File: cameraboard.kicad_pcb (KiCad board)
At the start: 4 copper layers, 47.2 x 46.8 mm, 93 parts, among them J1 USB_C_Receptacle_USB2.0, J2 02x05 M 1.27mm, J4 F32R-1A7H1-11024, J6 TFM-110-12-L-D-A, J7 FLE-107-01-G-DV-A, J8 USD-1040310811, Q1 SQ3495EV-T1, Q2 DMP6350SQ-7, SW1 CAS-120TA, SW2 KMR2x, SW4 CAS-120TA, U1 STM32H743VITx, U2 WE-TVS-82400102, U3 XC6210B332MR-G, U4 AP7366-28W5-7, U5 ?, U6 LTC4412xS6, Y1 16MHz

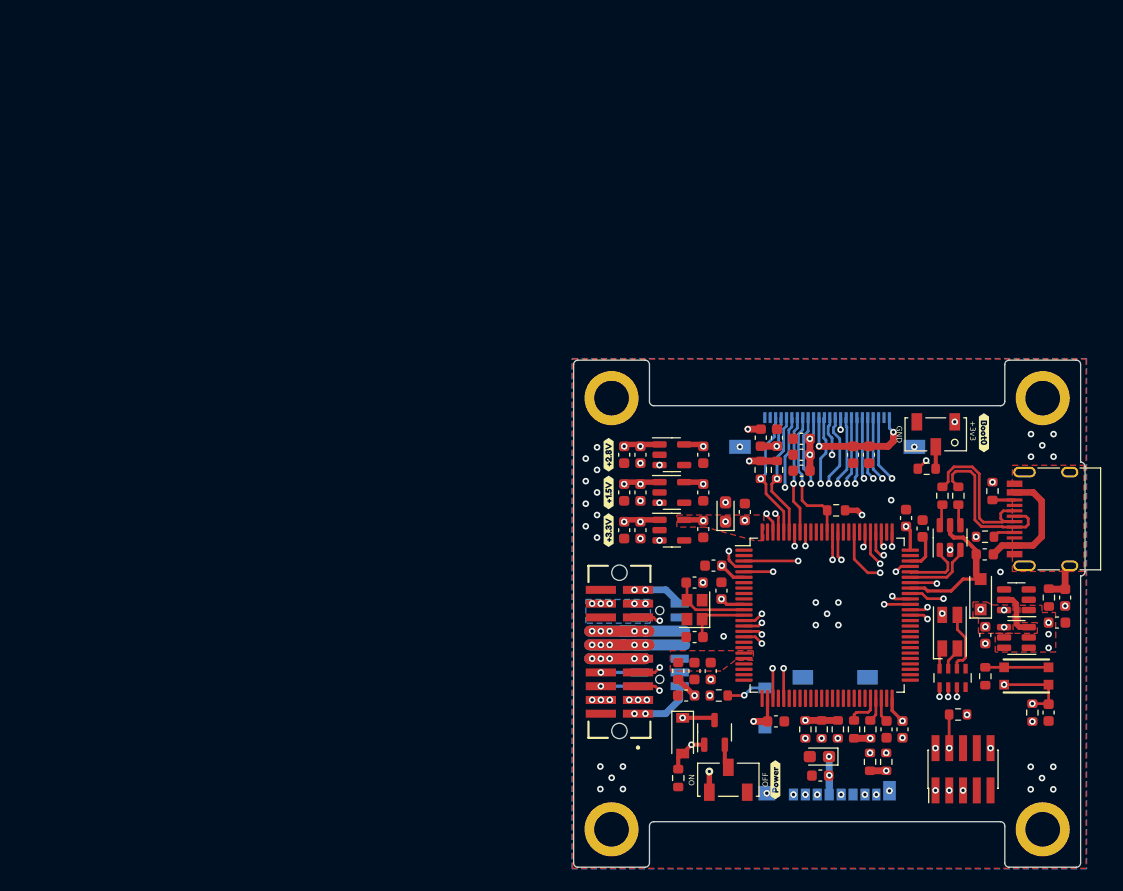
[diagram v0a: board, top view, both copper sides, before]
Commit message: Simplified Enable Circuit
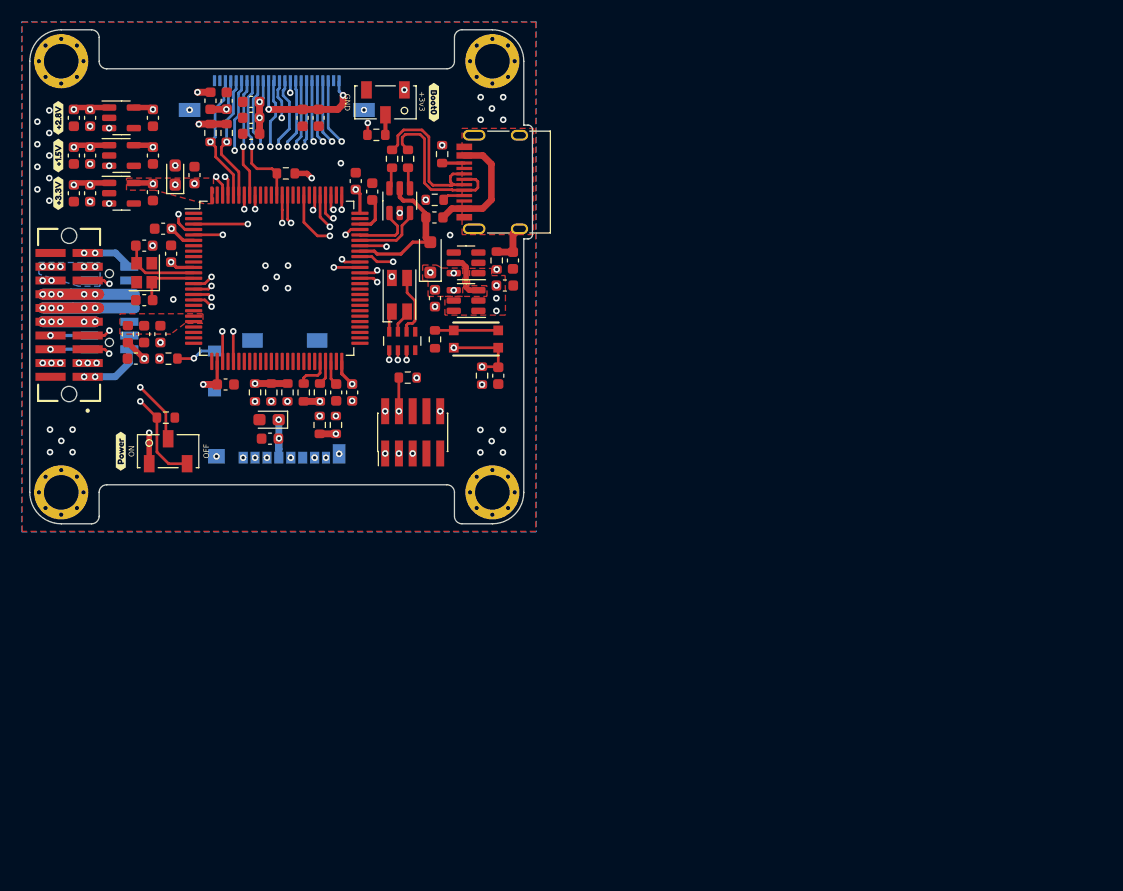
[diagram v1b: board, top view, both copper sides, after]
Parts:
- removed the D2 at (140.5, 108.6)
- removed Q2: DMP6350SQ-7, Package_TO_SOT_SMD:SOT-23-3
- J4: value F32R-1A7H1-11024 -> MOLEX_5051102491; footprint cameraboard:5051102491 -> cameraboard:MOLEX_5051102491
- J6: value TFM-110-12-L-D-A -> TFM-110-12-X-D-A; footprint cameraboard:SAMTEC_TFM-110-12-L-D-A -> mainboard:SAMTEC_TFM-110-12-X-D-A
- J7: value FLE-107-01-G-DV-A -> FLE-107-01-X-DV-A; footprint cameraboard:SAMTEC_FLE-107-01-G-DV-A -> cameraboard:SAMTEC_FLE-107-01-X-DV-A
- R9: value 100K -> 10K
- SW2: footprint mainboard:BTN_KMR2_4.6X2.8 -> mainboard:BTN_KMR2
- U5: value ? -> TLV75515PDBVR
- moved kibuzzard-63E3EAF3 67.6 mm to (88.6, 82.3)
- moved SW3 59.9 mm to (93.0, 82.3)
- moved C14 59.7 mm to (124.0, 67.0)
- moved C35 59.7 mm to (124.8, 64.7)
- moved R4 59.7 mm to (123.3, 64.7)
- moved C1 59.6 mm to (93.6, 56.8)
- moved C10 59.6 mm to (92.3, 71.5)
- moved C11 59.6 mm to (90.8, 71.5)
- moved C12 59.6 mm to (90.0, 73.8)
- moved C13 59.6 mm to (123.4, 75.3)
- moved C17 59.6 mm to (90.8, 68.4)
- moved C18 59.6 mm to (84.3, 58.5)
- moved C2 59.6 mm to (110.3, 57.4)
- moved C21 59.6 mm to (85.8, 58.5)
- moved C23 59.6 mm to (106.9, 51.5)
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- renumbered D3 to D2, SW4 to SW3
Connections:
- J4 pad P1: GND -> (no net)
- J4 pad P2: GND -> (no net)
- SW3 pad 2: Net-(SW4-Pad2) -> /POWER_EN
- SW3 pad 3: GND -> /PAYLOAD_EN
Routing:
- net /POWER_EN: track 27.2 -> 30.9 mm
- net /PAYLOAD_EN: track 18.8 -> 22.4 mm
- net Net-(SW4-Pad2): track 2.22 -> 0.00 mm
- net /HI_POW: track 11.2 -> 12.6 mm
- net /BOOT0: track 21.1 -> 19.9 mm
- net /BATT_P_SW: track 15.7 -> 14.9 mm
- net /DC+: track 15.6 -> 15.0 mm
- net /BATT_N_SW: track 17.0 -> 16.4 mm
- net /3V3_MB: track 11.5 -> 10.9 mm
- net GND: vias 57 -> 59
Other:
- board size 47.2 x 46.8 mm -> 46.4 x 45.6 mm
- board text added: "18-FEB-23"
- board text removed: "08-FEB-23"

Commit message: Stash before changes
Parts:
- R1: value 100 -> 100R
- R5, R8: value 22 -> 22R
- moved C19 8.84 mm to (111.1, 80.1), turned to -90 degrees
- moved R12 7.42 mm to (106.3, 82.1), turned to 0 degrees
- moved C20 7.22 mm to (109.5, 79.8), turned to 90 degrees
- moved R19 6.54 mm to (98.3, 77.6)
- moved R11 5.69 mm to (102.8, 79.1), turned to 0 degrees
- moved R13 5.30 mm to (106.3, 80.6), turned to 0 degrees
- moved R21 4.71 mm to (102.8, 77.6), turned to 0 degrees
- moved R20 3.18 mm to (106.3, 79.1), turned to 0 degrees
- moved J8 1.06 mm to (103.0, 78.5), turned to 90 degrees
- moved C4 0.36 mm to (108.1, 76.9)
- moved C3 0.36 mm to (109.6, 76.9)
- moved R17 0.33 mm to (106.7, 76.9)
- moved R15 0.31 mm to (105.2, 76.9)
- moved R10 0.18 mm to (115.3, 75.5)
- moved J2 0.15 mm to (115.7, 80.5)
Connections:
- J4 pad P1: (no net) -> GND
- J4 pad P2: (no net) -> GND
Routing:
- net /SDIO_D1: track 20.7 -> 31.1 mm, vias 3 -> 2
- net /SDIO_D0: track 20.7 -> 25.6 mm, vias 3 -> 2
- net /SDIO_D2: track 28.4 -> 32.9 mm, vias 3 -> 2
- net /SDIO_D3: track 28.0 -> 31.1 mm, vias 3 -> 2
- net /SDIO_CMD: track 28.3 -> 30.8 mm, vias 3 -> 2
- net +3.3V: track 31.6 -> 34.0 mm, vias 22 -> 24
- net /SD_CD: track 27.5 -> 28.9 mm, vias 2 -> 3
- net /SDIO_CLK: track 26.6 -> 25.4 mm
- net /SWCLK: track 24.4 -> 25.3 mm
- net GND: vias 59 -> 56

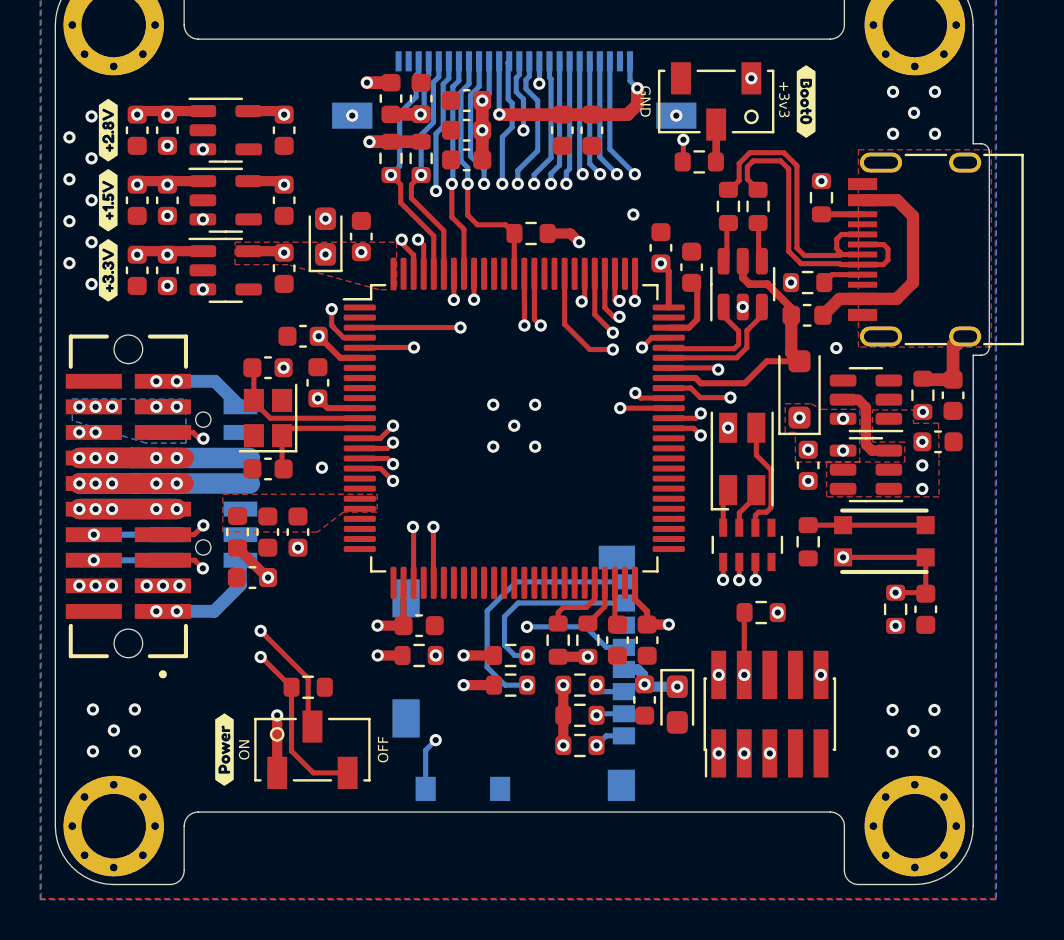
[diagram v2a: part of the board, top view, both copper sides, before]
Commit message: Moved SWD header and power switch to prevent mechanical interference
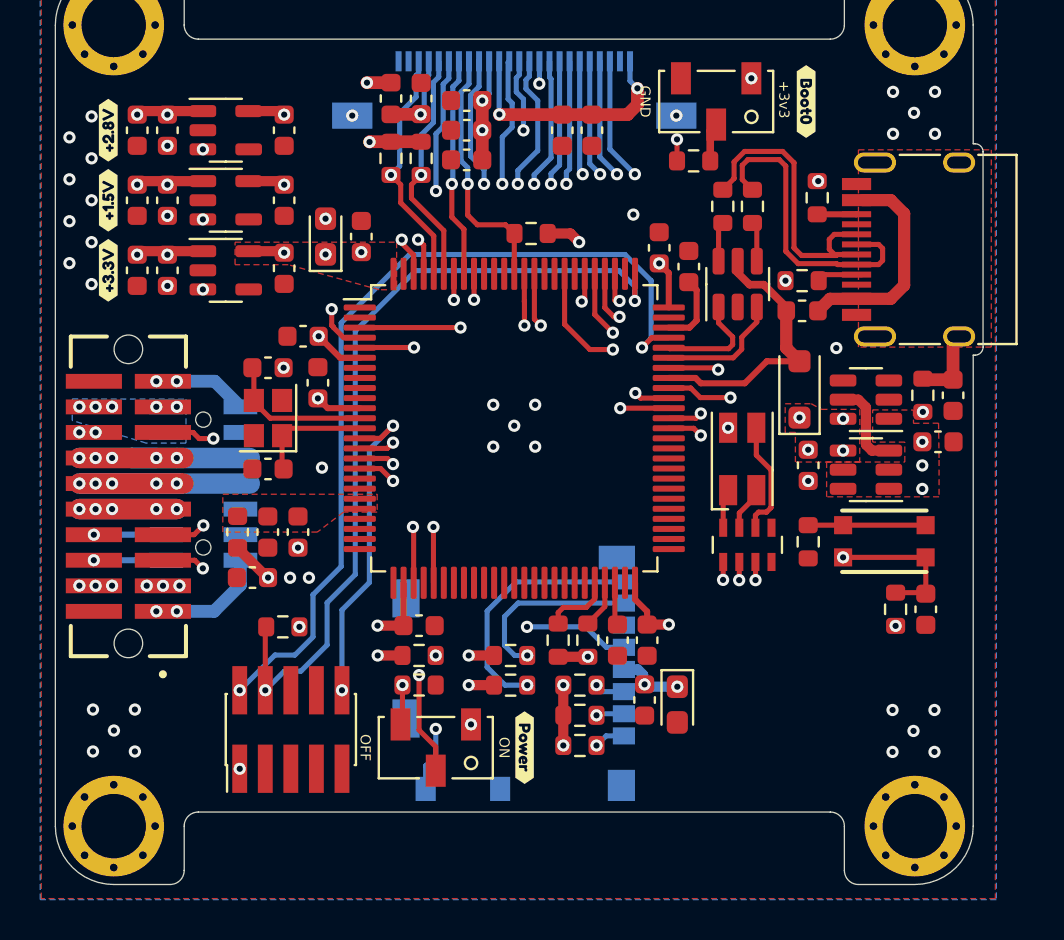
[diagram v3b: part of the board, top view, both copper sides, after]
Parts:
- moved J2 23.8 mm to (91.9, 81.3)
- moved R10 23.8 mm to (91.5, 76.2)
- moved kibuzzard-63E3EAF3 14.9 mm to (103.5, 82.2), turned to -90 degrees
- moved SW3 6.13 mm to (99.1, 82.2), turned to 180 degrees
- moved R9 5.51 mm to (98.3, 79.1)
- moved FB2 0.33 mm to (117.3, 60.5)
- moved J1 0.30 mm to (124.0, 57.5)
- moved R6 0.29 mm to (117.3, 59.0)
- moved R2 0.29 mm to (111.9, 53.0)
- moved R5 0.28 mm to (113.4, 55.3)
- moved R8 0.28 mm to (114.8, 55.3)
- moved U2 0.25 mm to (114.1, 59.2)
- moved R7 0.21 mm to (118.0, 54.9)
- moved C6 0.14 mm to (111.7, 58.3)
- moved C2 0.09 mm to (110.2, 57.4)
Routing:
- net /SWDIO: track 19.4 -> 43.3 mm
- net /SWCLK: track 25.3 -> 40.9 mm
- net /NRST: track 40.8 -> 48.5 mm, vias 4 -> 3
- net /POWER_EN: track 30.9 -> 36.0 mm, vias 4 -> 5
- net /HI_POW: track 12.6 -> 9.26 mm
- net /DC+: track 15.0 -> 16.4 mm
- net /PAYLOAD_EN: track 22.4 -> 21.3 mm, vias 2 -> 3
- net Net-(J1-SHIELD): track 3.79 -> 3.18 mm
- net Net-(FB2-Pad1): track 11.3 -> 10.7 mm
- net GND: vias 56 -> 53
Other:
- board size 46.4 x 45.6 mm -> 46.1 x 45.6 mm

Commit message: Exported Gerbers
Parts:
- renumbered J8 to J3, J6 to J5, J7 to J6
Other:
- board text added: "Bootloader"
- board text added: "MB Enable"
- board text added: "Normal"
- board text added: "On"
- board text removed: "+3v3"
- board text removed: "GND"
- board text removed: "OFF"
- board text removed: "ON"

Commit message: Rev B3/02 updates
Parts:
- removed the FB2 at (117.3, 60.5)
- removed the R5 at (113.4, 55.3)
- removed the R8 at (114.8, 55.3)
- added R20: 0R, Resistor_SMD:R_0603_1608Metric, F.Cu at (117.3, 60.5)
- added REF**: Fiducial_1mm_Mask2mm, Fiducial:Fiducial_1mm_Mask2mm, F.Cu at (122.9, 82.1)
- added REF**: Fiducial_1mm_Mask2mm, Fiducial:Fiducial_1mm_Mask2mm, F.Cu at (122.9, 50.3)
- added REF**: Fiducial_1mm_Mask2mm, Fiducial:Fiducial_1mm_Mask2mm, F.Cu at (83.1, 82.1)
- added REF**: Fiducial_1mm_Mask2mm, Fiducial:Fiducial_1mm_Mask2mm, B.Cu at (122.9, 50.3)
- added REF**: Fiducial_1mm_Mask2mm, Fiducial:Fiducial_1mm_Mask2mm, B.Cu at (122.9, 82.1)
- added REF**: Fiducial_1mm_Mask2mm, Fiducial:Fiducial_1mm_Mask2mm, B.Cu at (83.1, 82.1)
- C16, C17: value 10pF -> 4pF
- Ref**: moved to F.Cu
- Y1: value 16MHz -> 12MHz/7pF
- moved Ref** 18.3 mm to (116.2, 76.3)
- renumbered FB3 to FB2, R4 to R1, R20 to R10, R21 to R11, R11 to R12, R12 to R13, R13 to R14, R14 to R15, R15 to R17, R17 to R18, R18 to R19, R6 to R2, R7 to R3, R1 to R4, R3 to R5, R2 to R6, R9 to R7, R10 to R8, R19 to R9
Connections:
- J1 pad A6: /DC+ -> /D+
- J1 pad A7: /DC- -> /D-
- J1 pad B6: /DC+ -> /D+
- J1 pad B7: /DC- -> /D-
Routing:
- net /DC+: track 16.4 -> 0.00 mm
- net /DC-: track 15.2 -> 0.00 mm
- net /D+: track 1.99 -> 15.7 mm
- net /D-: track 1.69 -> 14.5 mm
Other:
- board text added: "12-APR-23"
- board text added: "Rev B3/02"
- board text removed: "18-FEB-23"
- board text removed: "Rev B3/01"

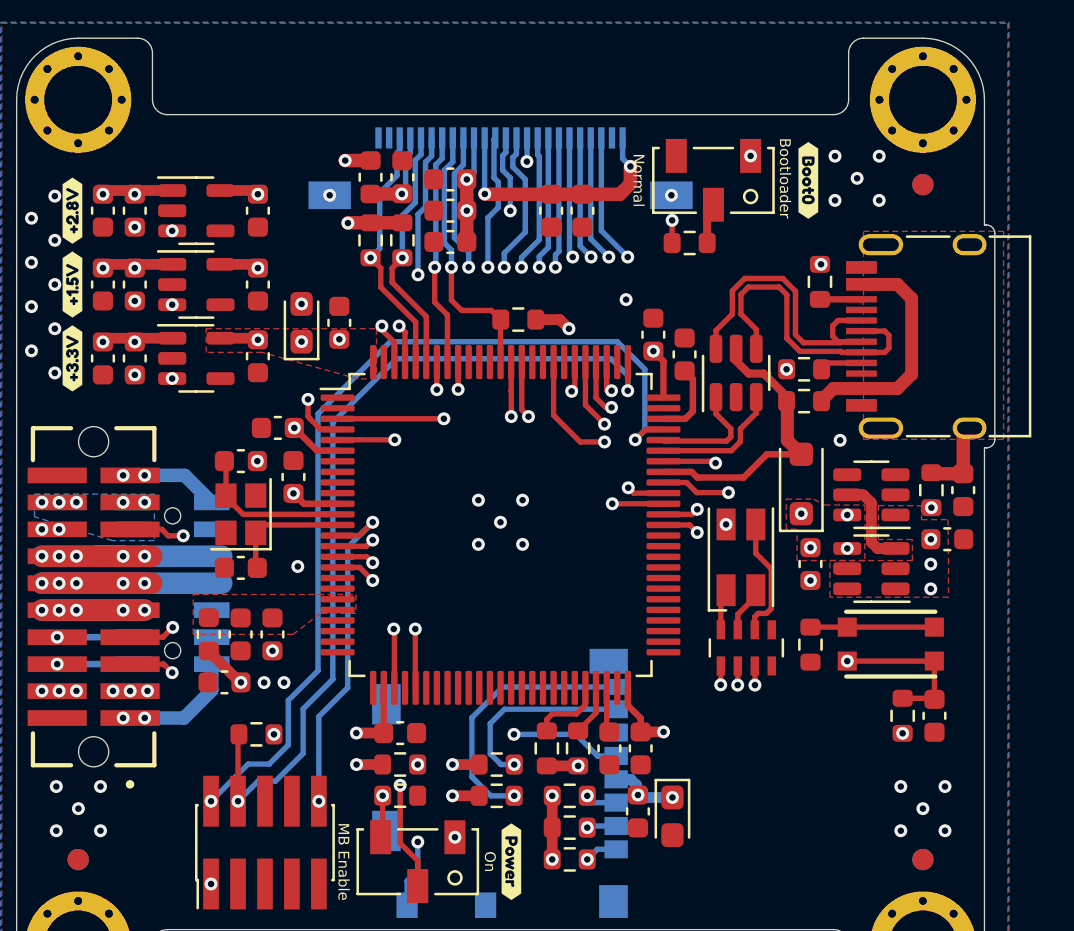
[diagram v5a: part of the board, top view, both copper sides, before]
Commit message: Rewired UART lines to mainboard
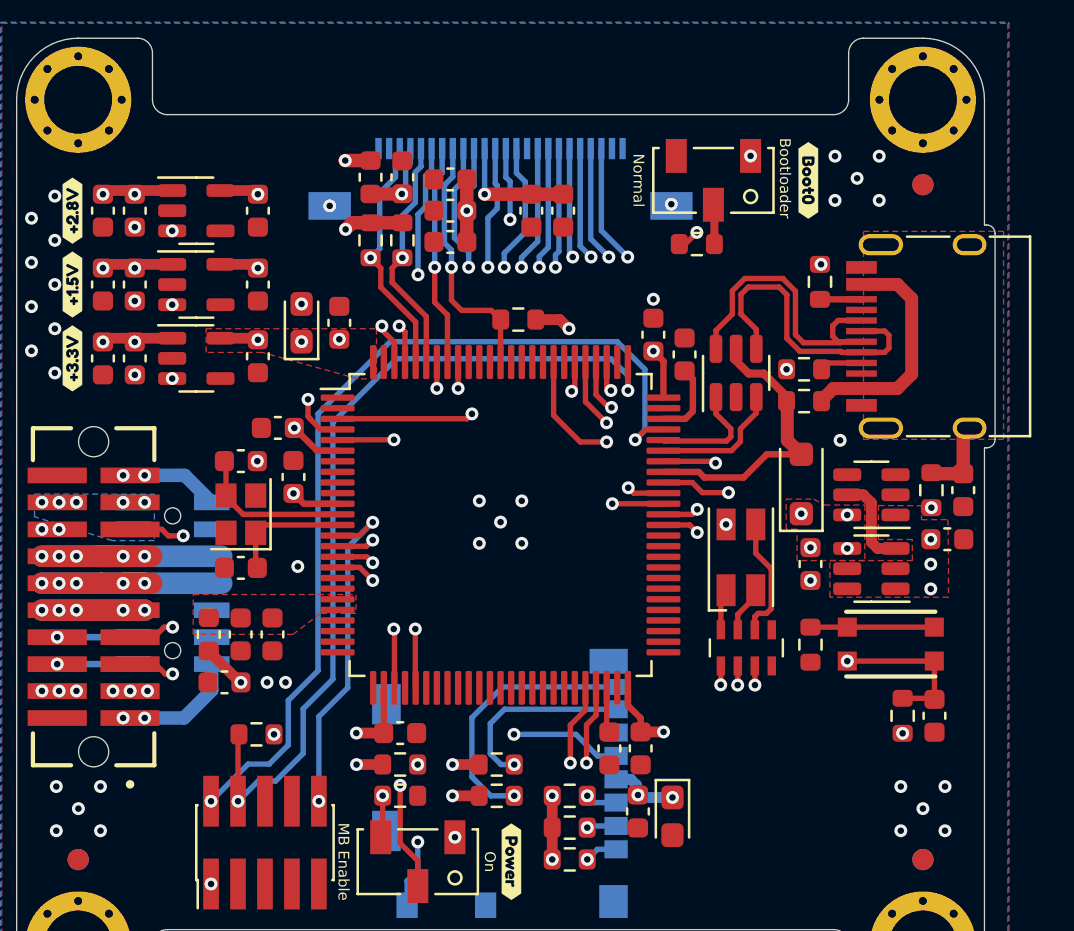
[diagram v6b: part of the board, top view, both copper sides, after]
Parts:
- removed R17, R18: 4.7K, Resistor_SMD:R_0603_1608Metric
- R15, R16: value 4.7K -> 10K
- moved C22 0.93 mm to (104.5, 51.5)
- moved C23 0.91 mm to (106.0, 51.5)
- moved J4 0.50 mm to (103.0, 51.1)
- moved R6 0.34 mm to (112.2, 53.1)
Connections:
- J4 pad 1: 2.8V -> unconnected-(J4-Pin_1-Pad1)
- J4 pad 2: GND -> unconnected-(J4-Pin_2-Pad2)
- J5 pad 5: /UART2_RX -> /UART3_RX
- J5 pad 7: /UART2_TX -> /UART3_TX
- U1 pad 46: /I2C2_SCL -> /UART3_TX
- U1 pad 47: /I2C2_SDA -> /UART3_RX
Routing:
- net /UART2_RX: track 29.9 -> 0.00 mm, vias 2 -> 0
- net /UART3_RX: track 0.00 -> 29.0 mm, vias 0 -> 2
- net /UART3_TX: track 0.00 -> 27.4 mm, vias 0 -> 2
- net /UART2_TX: track 26.9 -> 0.00 mm, vias 2 -> 0
- net 2.8V: track 14.8 -> 8.63 mm, vias 4 -> 3
- net /I2C2_SCL: track 3.45 -> 0.00 mm
- net /I2C2_SDA: track 2.38 -> 0.00 mm
- net +3.3V: track 33.5 -> 32.3 mm, vias 24 -> 23
- net GND: track 1.12 -> 0.00 mm, vias 53 -> 51
- net /BOOT0: track 20.0 -> 18.9 mm
- net 1.5V: track 6.63 -> 7.60 mm, vias 3 -> 2
- net /DCMI_D2: track 20.5 -> 19.6 mm
- net /DCMI_D6: track 23.3 -> 22.4 mm
- net /DCMI_D3: track 19.6 -> 18.8 mm
- net /DCMI_D5: track 14.8 -> 14.1 mm
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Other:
- board text added: "12-JUN-23"
- board text added: "Rev B3/03"
- board text removed: "12-APR-23"
- board text removed: "Rev B3/02"
